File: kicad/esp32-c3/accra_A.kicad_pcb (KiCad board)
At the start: 6 copper layers, 72 x 42 mm, 35 parts, among them IC1 ESP32-C3-WROOM-02-H4, J1 Conn_01x04_Male, J2 Conn_01x04_Male, J3 Conn_02x04_Counter_Clockwise, J4 Conn_01x12_Male, J5 Conn_01x04, SW1 ALPS SKHH, U1 R-78C3.3-1.0, U2 SN65HVD232

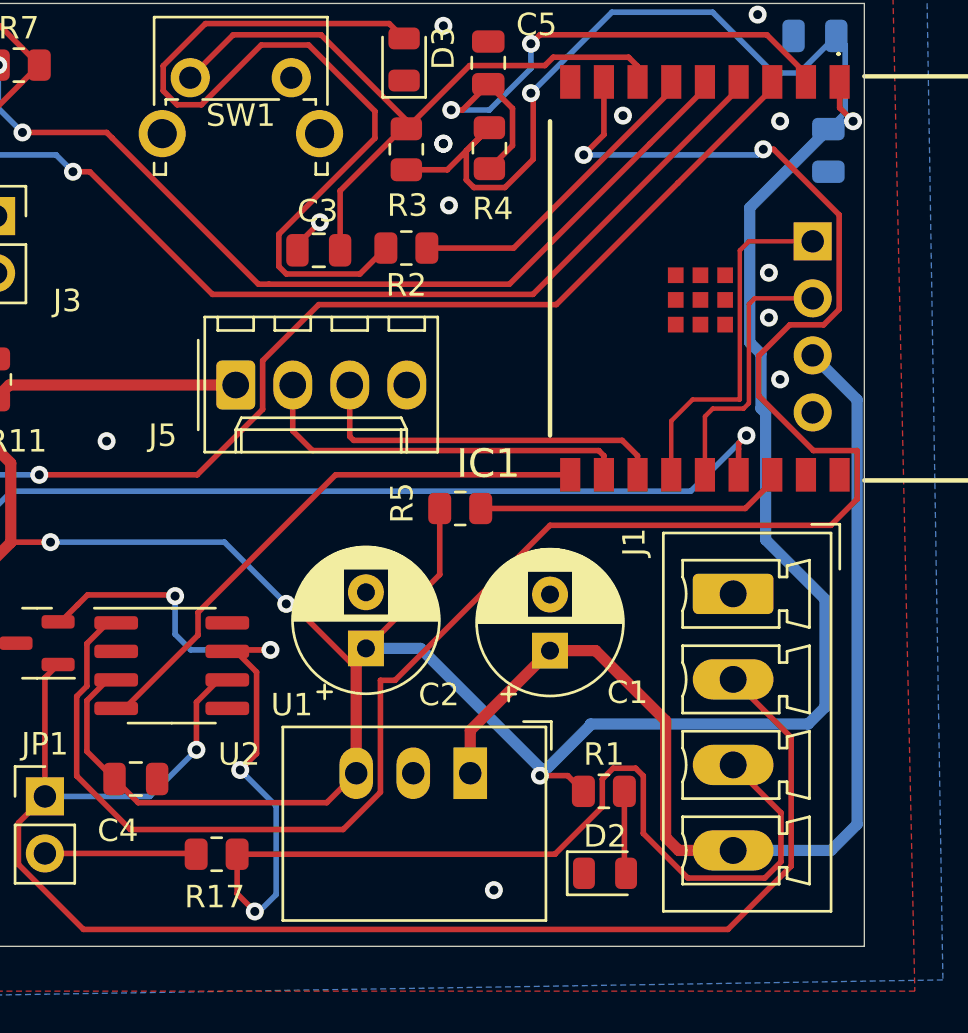
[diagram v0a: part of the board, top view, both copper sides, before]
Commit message: Changes power caps to SMD
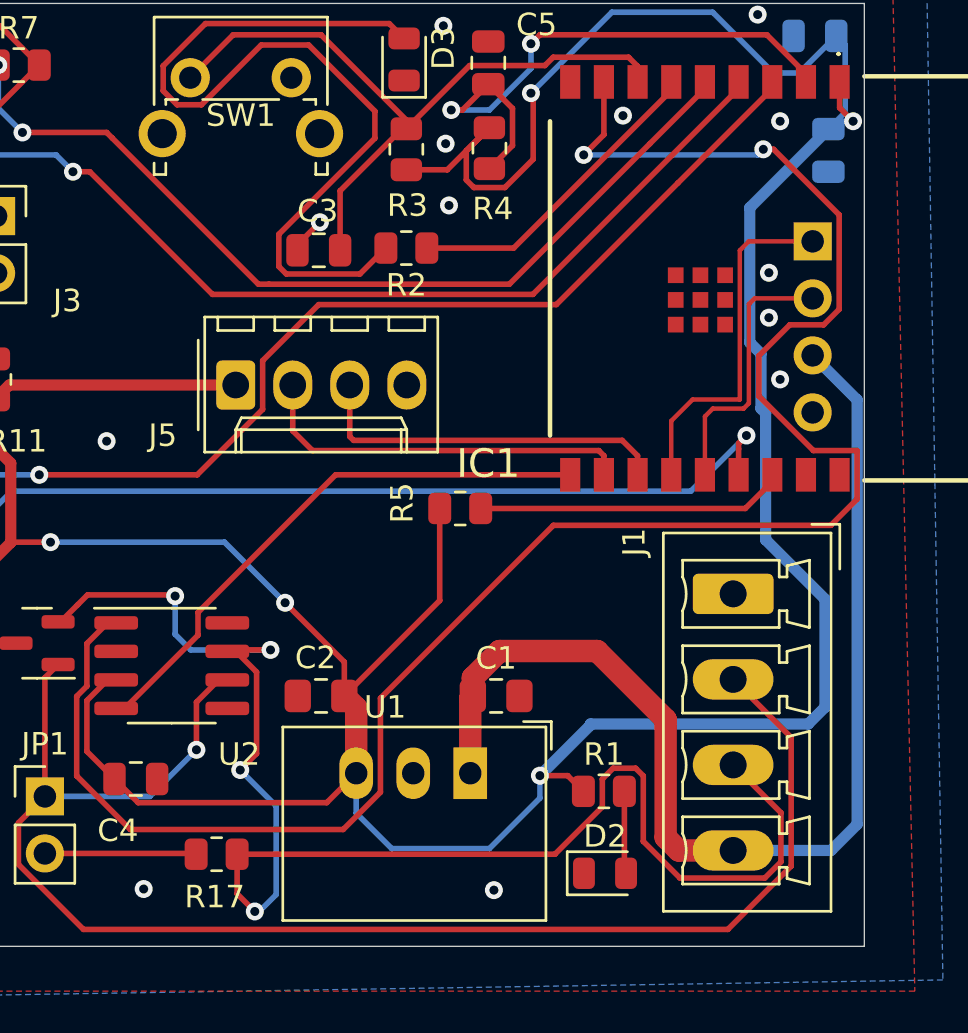
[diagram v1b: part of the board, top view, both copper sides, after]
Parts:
- C1, C2: footprint Capacitor_THT:CP_Radial_D6.3mm_P2.50mm -> Capacitor_SMD:C_0805_2012Metric_Pad1.18x1.45mm_HandSolder
- moved C1 3.14 mm to (168.1, 114.8), turned to 0 degrees
- moved C2 2.91 mm to (160.3, 114.8), turned to 180 degrees
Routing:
- net +28V: track 49.5 -> 50.9 mm
- net +3V3: track 272.1 -> 271.0 mm

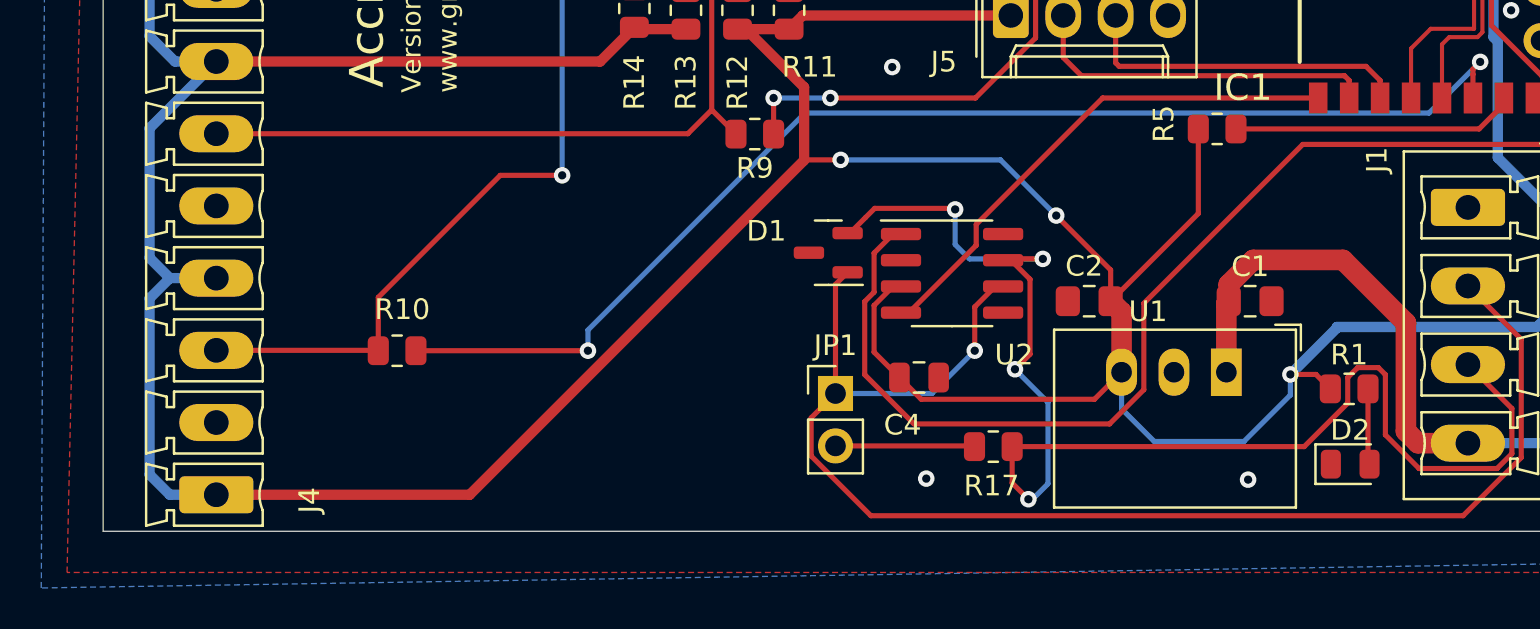
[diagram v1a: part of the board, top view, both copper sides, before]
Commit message: Added protection diod on input
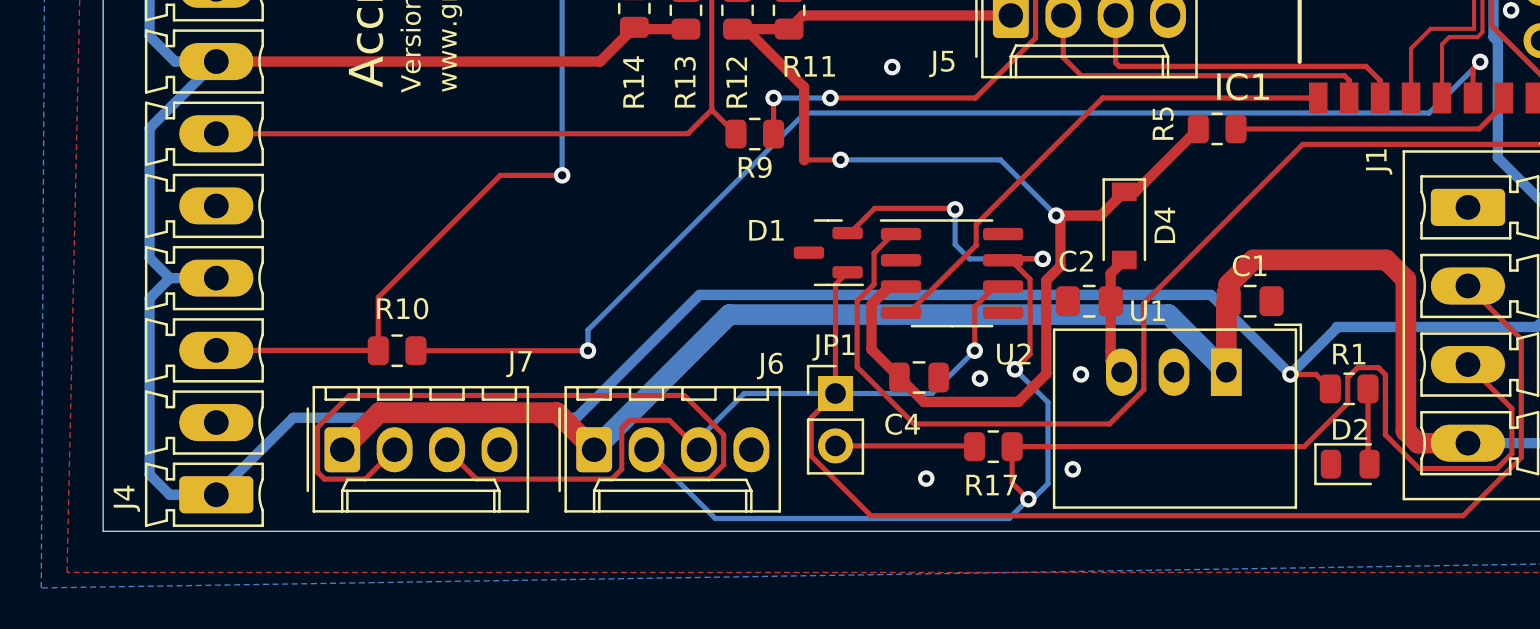
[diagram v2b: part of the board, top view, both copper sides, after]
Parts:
- added D4: 1N5819, Diode_SMD:D_SOD-123, F.Cu at (162.0, 111.2)
- added J6: Conn_01x04, Connector_Molex:Molex_KK-254_AE-6410-04A_1x04_P2.54mm_Vertical, F.Cu at (136.3, 122.0)
- added J7: Conn_01x04, Connector_Molex:Molex_KK-254_AE-6410-04A_1x04_P2.54mm_Vertical, F.Cu at (124.1, 122.0)
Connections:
- net Net-(D1-Pad1) renamed /CANL
- net Net-(D1-Pad2) renamed /CANH
- C2 pad 1: +3V3 -> Net-(C2-Pad1)
- U1 pad 3: +3V3 -> Net-(C2-Pad1)
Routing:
- net /CANH: track 66.4 -> 120.5 mm
- net +28V: track 50.9 -> 100.3 mm
- net /CANL: track 67.3 -> 91.1 mm
- net Net-(C2-Pad1): track 0.00 -> 6.23 mm
- net +3V3: track 271.0 -> 275.6 mm
- net GND: vias 13 -> 15

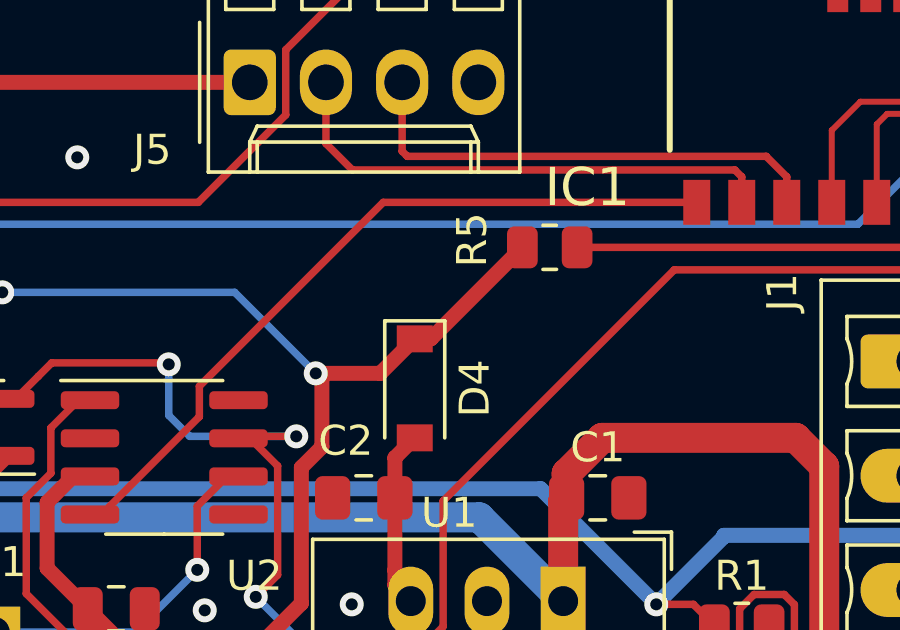
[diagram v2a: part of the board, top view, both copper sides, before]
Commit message: Closed open ground plane
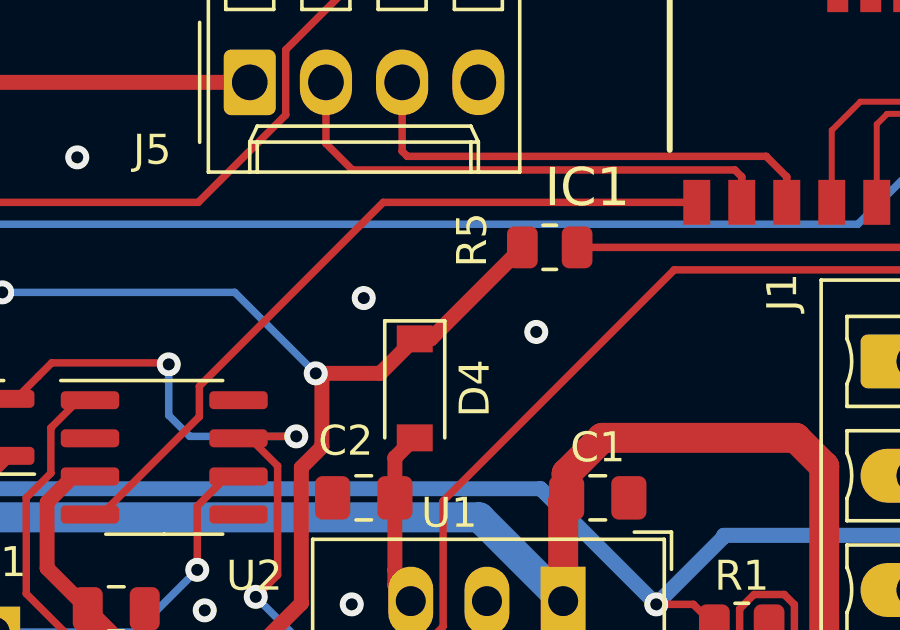
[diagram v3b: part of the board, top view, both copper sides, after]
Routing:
- net GND: vias 15 -> 17
